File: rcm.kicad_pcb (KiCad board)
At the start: 2 copper layers, 140 x 70 mm, 158 parts, among them Y1 8MHz, Y2 32.768kHz

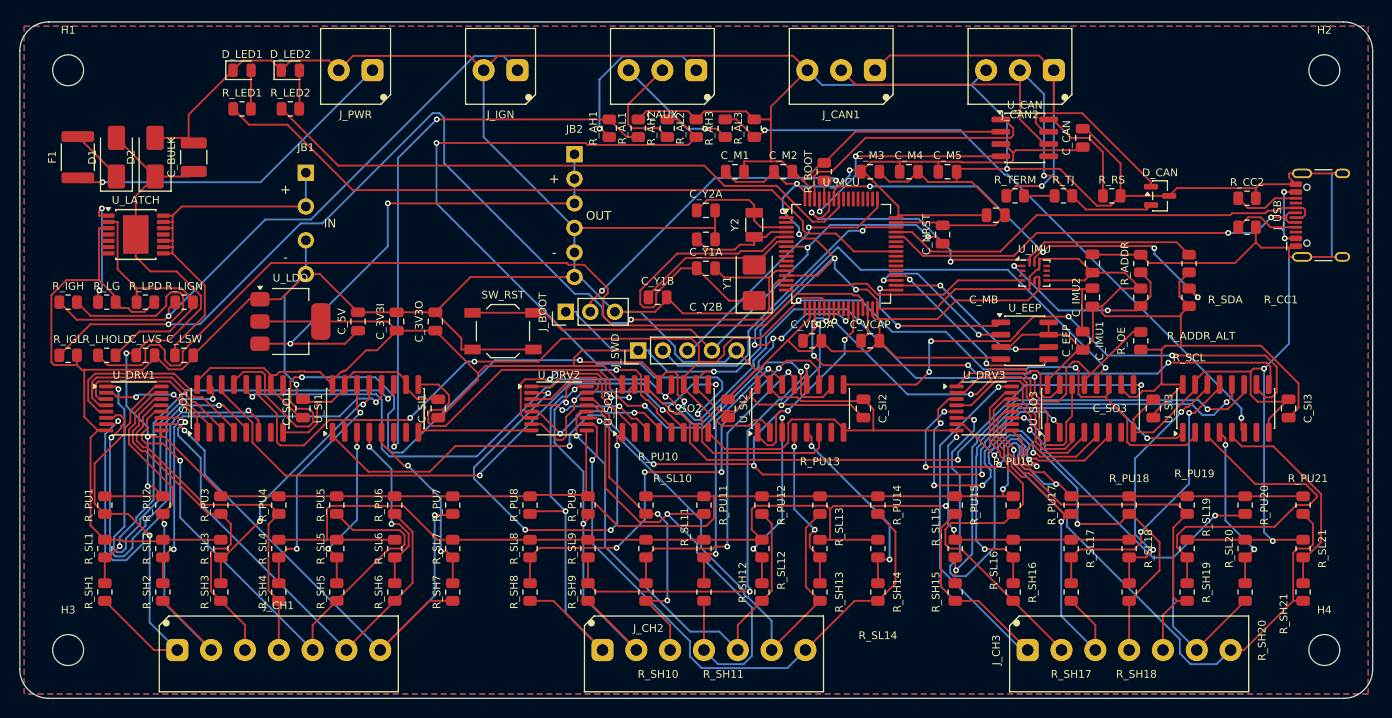
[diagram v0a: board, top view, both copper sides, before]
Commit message: rcm: resistor rows re-ordered, BOM sourced, manufacturing files out
Placement (user request): the three southern resistor rows keep their
6.0/10.5/15.0mm centre spacing, but R_PU moves to the southern row and
R_SH to the middle, both at rotation 0, with R_SL to the north row at
180. Laying them flat cleared nearly all the silkscreen crowding in the
south tiles.

BOM sourcing is complete - every line that gets assembled now has an
LCSC number. Four substitutions came out of it and are folded back into
gen_spec.py so the schematic agrees rather than the choice living only
in a side file:

  - AMS1117-3.3 for LD1117S33: JLC basic part, and pin-identical by
    construction (both symbols extend AP1117-15).
  - M95640 for 25LC640: $0.33 against $0.73-1.42 and better stocked,
    same 25-series SPI pinout the generic symbol already describes.
  - 60V PPTC over 30V: the SMAJ33A clamps near 53V.
  - 20pF for 12pF crystal load caps. This one was a genuine error, not
    a cost change: the 12.5pF crystal wants ~19pF, and 12pF ran the RTC
    about 22ppm fast - a minute a month. Also deletes a BOM line.

jlc_parts.json is rekeyed to 'value|footprint', which is what the BOM
script actually looks up; keyed by bare value it silently matched
nothing and would have produced an entirely unsourced BOM. The
footprint half earned its keep immediately by catching that the cheap
basic 8MHz crystal is HC-49S-SMD and would not fit the 5032 lands.
gen_spec.py now stamps an LCSC field onto every symbol from that same
file, and fails the build if a component has no line.

Two new shared tools: shrink_refs.py (0.8mm ref text on crowded parts,
which is what lets relocate_refs converge) and fix_marginal_clearance.py
(narrow rather than move segments that miss a rule by microns).

Board: 414/414 routed, 0 unconnected, 0 schematic parity. One clearance
violation survives at 1.3 microns short - deterministic, understood, and
documented in SPEC.md along with the three rejected fixes.

Gerbers export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
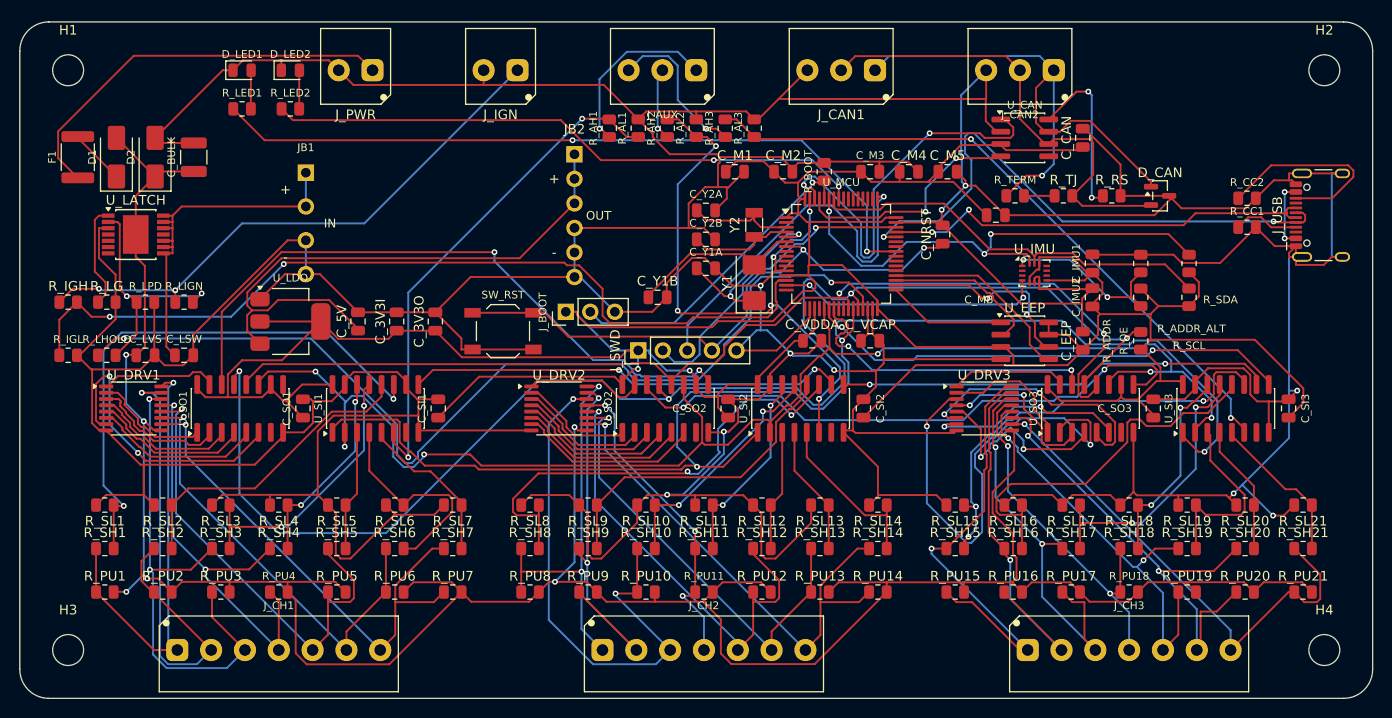
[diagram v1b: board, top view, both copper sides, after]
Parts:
- C_Y2A, C_Y2B: value 12pF -> 20pF
- U_EEP: value 25LC640 -> M95640
- U_LDO: value LD1117S33 -> AMS1117-3.3
- moved R_PU1 9.00 mm to (8.80, 59.0), turned to 0 degrees
- moved R_PU10 9.00 mm to (64.8, 59.0), turned to 0 degrees
- moved R_PU11 9.00 mm to (70.8, 59.0), turned to 0 degrees
- moved R_PU12 9.00 mm to (76.8, 59.0), turned to 0 degrees
- moved R_PU13 9.00 mm to (82.8, 59.0), turned to 0 degrees
- moved R_PU14 9.00 mm to (88.8, 59.0), turned to 0 degrees
- moved R_PU15 9.00 mm to (96.8, 59.0), turned to 0 degrees
- moved R_PU16 9.00 mm to (102.8, 59.0), turned to 0 degrees
- moved R_PU17 9.00 mm to (108.8, 59.0), turned to 0 degrees
- moved R_PU18 9.00 mm to (114.8, 59.0), turned to 0 degrees
- moved R_PU19 9.00 mm to (120.8, 59.0), turned to 0 degrees
- moved R_PU2 9.00 mm to (14.8, 59.0), turned to 0 degrees
- moved R_PU20 9.00 mm to (126.8, 59.0), turned to 0 degrees
- moved R_PU21 9.00 mm to (132.8, 59.0), turned to 0 degrees
- moved R_PU3 9.00 mm to (20.8, 59.0), turned to 0 degrees
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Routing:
- net +12V_P: track 220.1 -> 276.6 mm, vias 5 -> 6
- net ASNS2: track 96.4 -> 52.7 mm, vias 2 -> 4
- net DRV1: track 42.8 -> 12.0 mm, vias 2 -> 0
- net DRV9: track 40.8 -> 11.8 mm, vias 4 -> 0
- net IGN_SENSE: track 118.1 -> 90.4 mm
- net DRV6: track 44.2 -> 17.6 mm, vias 2 -> 0
- net GND: track 897.8 -> 873.1 mm, vias 7 -> 12
- net DRV20: track 50.9 -> 26.4 mm
- net SR_RCLK: track 133.6 -> 110.1 mm, vias 8 -> 2
- net CH10: track 33.7 -> 55.4 mm
- net +3V3: track 370.1 -> 391.5 mm, vias 9 -> 2
- net DRV17: track 30.7 -> 49.7 mm, vias 4 -> 2
- net CH11: track 51.1 -> 33.1 mm, vias 1 -> 3
- net CH3: track 35.8 -> 53.5 mm, vias 0 -> 2
- net SR_DI12: track 61.8 -> 45.5 mm
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- removed copper zone on B.Cu, net GND
- removed copper zone on F.Cu, net GND

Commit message: rcm: restore the GND pour - round 3 was routed without --zone
route_board.py's --zone defaults to empty, so omitting it produced a
fully routed, 0-unconnected, DRC-clean board with no copper pour on
either layer. Nothing in any report flagged it: an absent zone violates
no design rule, so DRC, the router summary and the netlist round-trip
were all clean and all silent. Caught by eye off the 3D view.

Re-routed with --zone GND:F.Cu --zone GND:B.Cu (2 zones, both filled,
33 polygons), then fix_starved_thermals.py set J_USB.A12, J_USB.B1 and
U_MCU.47 solid where thermal spokes came up short.

Board is otherwise where it was: 414/414 routed, 0 unconnected, 0
schematic parity, 26 silkscreen warnings and the same understood 1.3
micron clearance miss - which recurring across yet another independent
route further confirms it is deterministic geometry, not router noise.

Gerbers, BOM and CPL regenerated against the poured board; the previous
set had stale copper layers. Copper gerbers now carry the pour as G36
regions (F.Cu 27, B.Cu 6) and the zip goes 120kB -> 280kB.

Documented in CLAUDE.md and SPEC.md, including how to verify the pour
exists - counting top-level zone blocks, not the string '(zone', which
also matches the zone_connect inside every pad.

Co-Authored-By: Claude Opus 5 <noreply@anthropic.com>
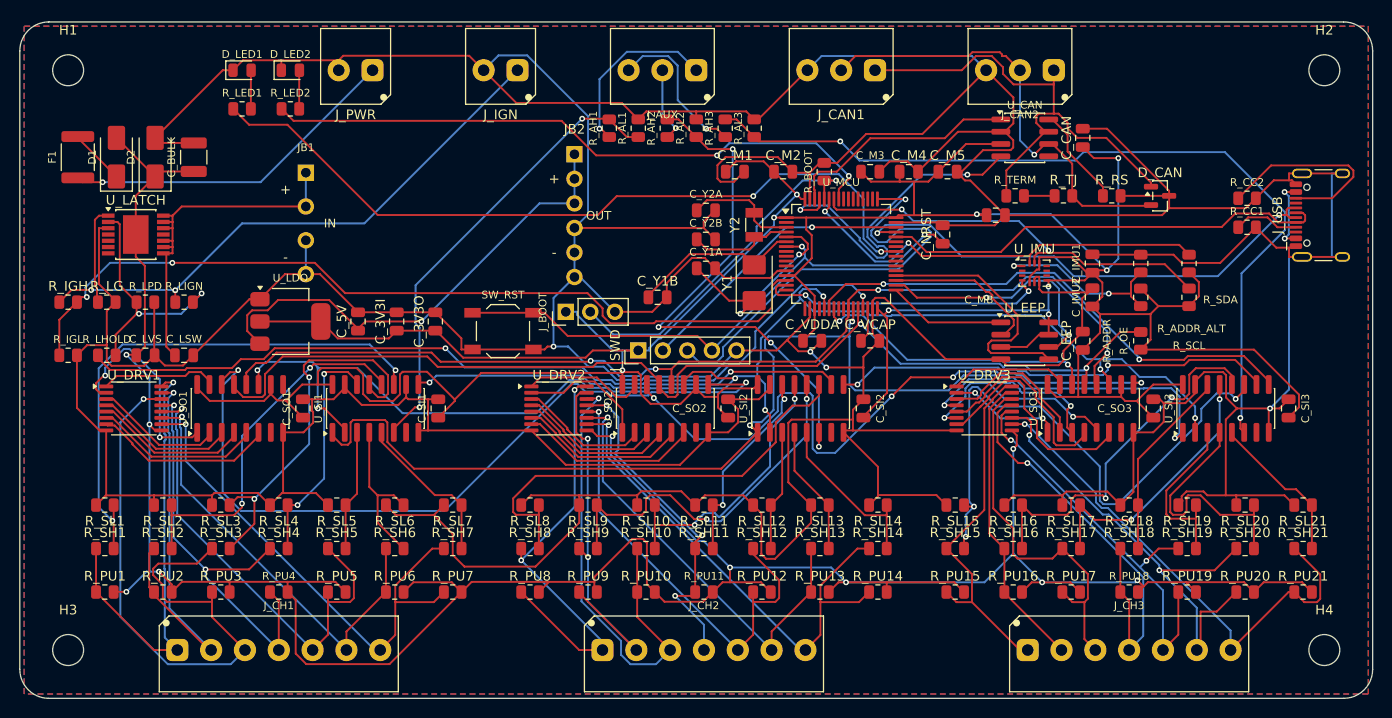
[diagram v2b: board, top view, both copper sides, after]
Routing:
- net SR_OE_N: track 149.5 -> 111.7 mm, vias 4 -> 2
- net DRV17: track 49.7 -> 15.8 mm, vias 2 -> 0
- net ASNS3: track 68.5 -> 87.5 mm
- net SR_PL: track 140.1 -> 122.3 mm
- net CAN_TX: track 41.7 -> 24.2 mm, vias 2 -> 0
- net SNS15: track 45.6 -> 60.5 mm
- net GND: track 873.1 -> 887.3 mm, vias 12 -> 4
- net SR_CH21: track 67.7 -> 81.3 mm
- net +12V_P: track 276.6 -> 289.9 mm, vias 6 -> 10
- net SNS20: track 13.5 -> 26.3 mm
- net USB_DM: track 58.9 -> 46.7 mm, vias 2 -> 0
- net LATCH_HOLD: track 101.5 -> 89.4 mm
- net +5V: track 61.9 -> 49.9 mm, vias 0 -> 1
- net DRV7: track 30.1 -> 18.8 mm, vias 2 -> 0
- net CAN_RX: track 24.3 -> 35.5 mm
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- added copper zone on B.Cu, net GND
- added copper zone on F.Cu, net GND

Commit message: rcm: latch part -> BTS7040-1EPZ, C534837 went to zero stock
JLC's quote priced 38 of 39 BOM lines; C534837 (BTS7040-1EPA) is
unbuyable. Swapped to C534838, BTS7040-1EPZ: same base part number, so
the Z is a temperature/variant grade rather than a different die and the
pinout is near-certain rather than resting on family convention. Same
PG-TSDSO-14-22 package, and better on both specs that matter - 19mOhm
against 36, and -40..+175C against +150.

The RCM:BTS70xx-1E symbol was built as a generic family part, which is
what made this a value-string change rather than a re-layout.

Stock is thin at ~10 pieces - enough for this run of 5 with spares. If it
goes, fall back to C534825 BTS7004-1EPP (~20k stock, overkill at
4.4mOhm/15A but harmless, same package and family pinout), which would
want a datasheet pinout check since it is not the same base part.

Rebuilt and re-routed WITH --zone GND:F.Cu --zone GND:B.Cu this time.
414/414 routed, 0 unconnected, 0 schematic parity, 2 filled GND pours,
and five pads set solid where thermal spokes came up short.

The 1.3 micron clearance miss is gone - this route avoids it - so the
board is now clean of every non-silkscreen violation, leaving 26 cosmetic
silkscreen warnings. That also corrects the earlier reading of it as
deterministic geometry: it was route-dependent, just not across the
routes tried at the time.

Gerbers, BOM and CPL regenerated.

Co-Authored-By: Claude Opus 5 <noreply@anthropic.com>
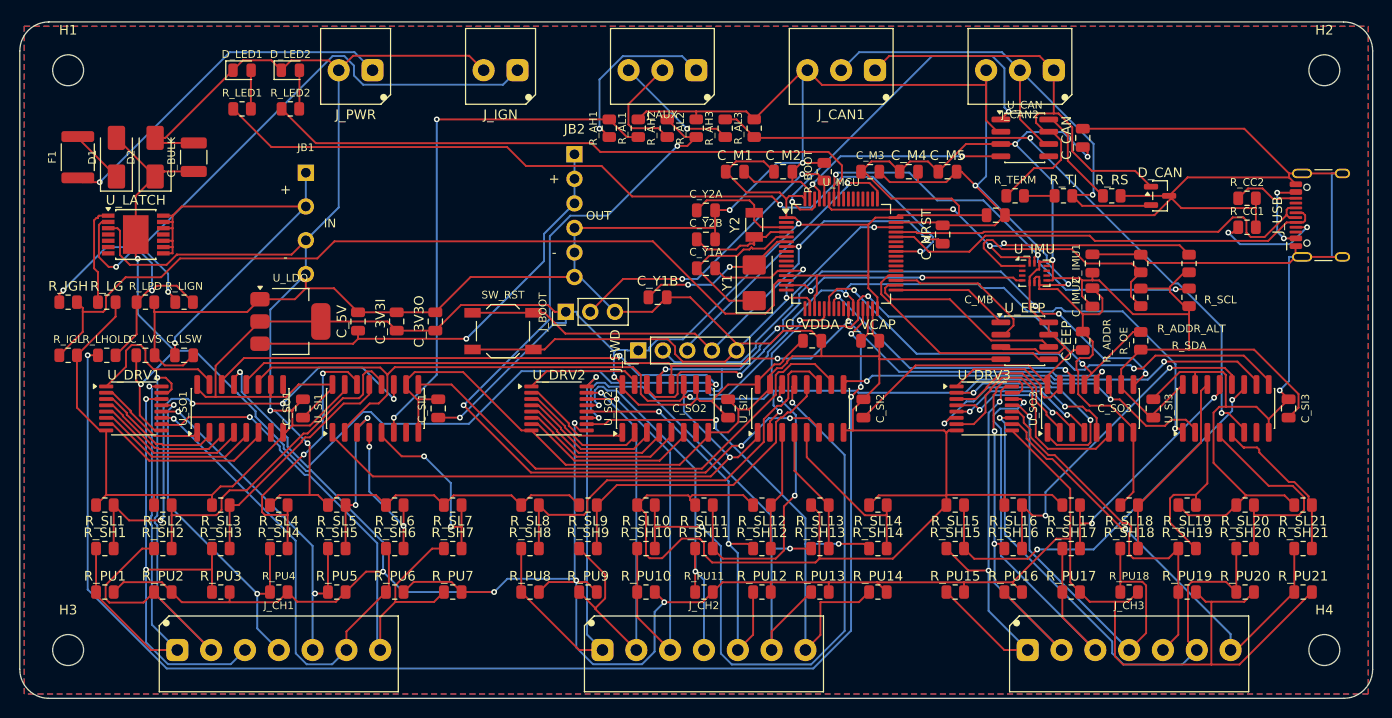
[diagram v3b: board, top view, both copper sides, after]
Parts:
- U_LATCH: value BTS7040-1EPA -> BTS7040-1EPZ
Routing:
- net GND: track 887.3 -> 944.1 mm, vias 4 -> 9
- net LATCH_HOLD: track 89.4 -> 144.0 mm, vias 2 -> 4
- net SNS10: track 28.9 -> 65.8 mm
- net ASNS2: track 56.2 -> 87.2 mm
- net SR_CH21: track 81.3 -> 54.7 mm
- net +12V_P: track 289.9 -> 311.0 mm, vias 10 -> 7
- net SWCLK: track 47.6 -> 28.5 mm
- net +3V3: track 397.7 -> 379.5 mm, vias 9 -> 6
- net SNS15: track 60.5 -> 42.3 mm, vias 3 -> 2
- net SR_OE_N: track 111.7 -> 127.3 mm, vias 2 -> 5
- net SNS3: track 39.9 -> 24.8 mm, vias 2 -> 0
- net ASNS3: track 87.5 -> 72.7 mm
- net CAN_TX: track 24.2 -> 38.5 mm, vias 0 -> 2
- net USB_CC2: track 21.1 -> 6.86 mm
- net CH3: track 64.0 -> 49.9 mm, vias 1 -> 2
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
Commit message: rcm: channel mode becomes a software table; add config DIP switch
Abandons the 21-DIP-switch plan and makes the board simpler instead.

The blocker was only ever the pull-UP: R_PU as 10k to +12V makes a blown
fuse read 2.531V and a good one 2.551V - both HIGH, 20mV apart, fuse
sensing dead. A 10k pull-DOWN does not, because the ~85 ohm relay coil
swamps it. All four states then read correctly with the SAME resistor
fitted on every channel:

  output, fuse good   2.530V HIGH      input, button open    0.000V LOW
  output, fuse blown  0.000V LOW       input, button closed  2.551V HIGH

So nothing is mode-dependent, there is nothing for hardware to select,
and in/out is purely a firmware table. R_PU is now fitted 10k to GND on
all 21 channels. That deleted the DIP array, the readback, the P-FET
rails and the south-half re-layout in one go.

Trade: buttons are positive-switched to +12V. Wetting current goes to
1.20mA (against 0.0094mA on the divider alone), and a chafed button wire
now reads 'not pressed' rather than phantom-activating.

Adds SW_CFG, one 8-way 1.27mm DIP in the top-right corner - the only free
10x10mm pocket, and next to J_CAN2 where the termination pole must reach.
Pos 1 CAN termination (passive, parallels R_TJ); pos 2-6 role, address
x2, bitrate, IMU publish enable, on PC0-PC4 using the STM32's internal
pull-ups so no external resistors are needed. These are the settings that
cannot be fixed over the bus once wrong.

Positions 7-8 are left unconnected deliberately: routing two more nets
from that corner across the CAN/IMU corridor is what tipped the board
from routable to not (3 nets failed, then 1). Dropping them fixed it.

426/426 routed, 0 unconnected, 0 schematic parity, 2 filled GND pours,
25 cosmetic silkscreen warnings and no electrical violations at all.
BOM 40 lines all sourced, CPL 149 placements.

VERIFY the DIP land before ordering - standard 1.27mm 8-position
gull-wing footprint, part not checked against a drawing.

Co-Authored-By: Claude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
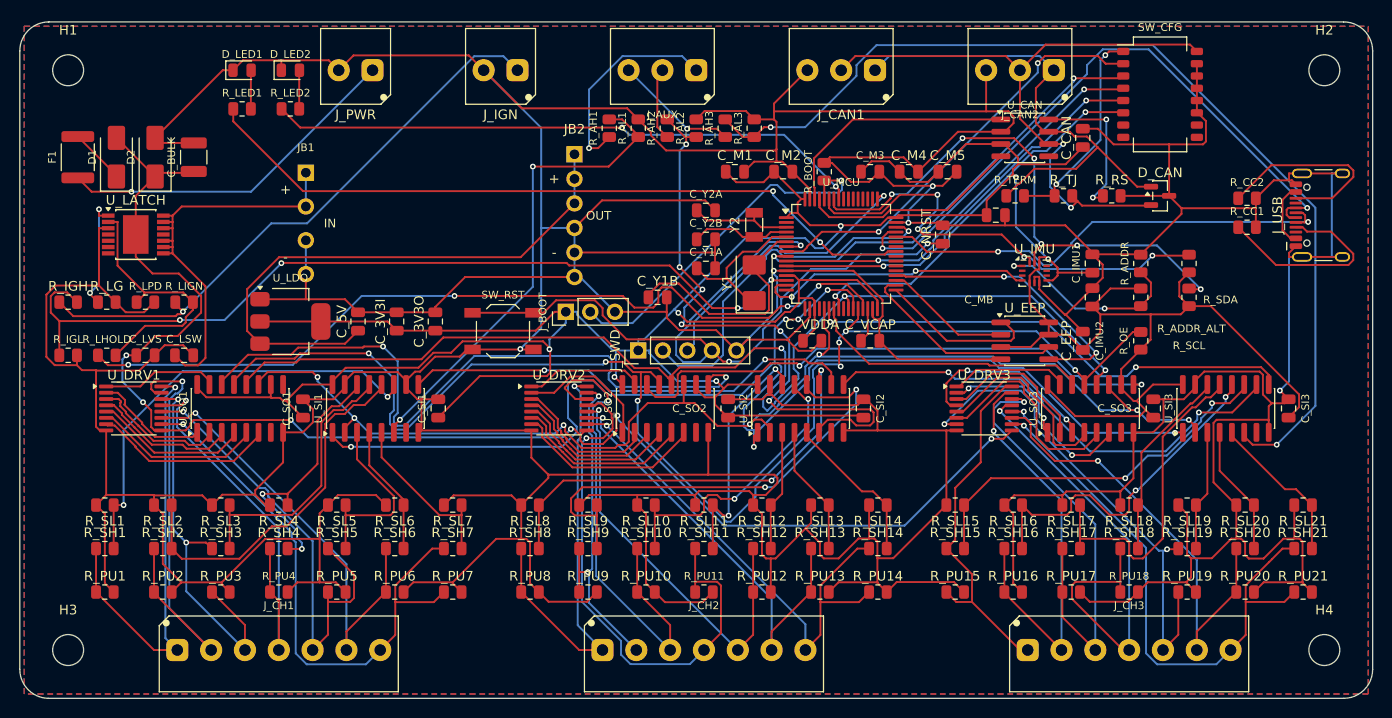
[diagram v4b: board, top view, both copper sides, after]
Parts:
- added SW_CFG: CFG_DIP, Button_Switch_SMD:SW_DIP_SPSTx08_Slide_KingTek_DSHP08TS_W7.62mm_P1.27mm, F.Cu at (118.0, 7.50)
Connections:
- R_PU1 pad 2: +12V_P -> GND
- R_PU10 pad 2: +12V_P -> GND
- R_PU11 pad 2: +12V_P -> GND
- R_PU12 pad 2: +12V_P -> GND
- R_PU13 pad 2: +12V_P -> GND
- R_PU14 pad 2: +12V_P -> GND
- R_PU15 pad 2: +12V_P -> GND
- R_PU16 pad 2: +12V_P -> GND
- R_PU17 pad 2: +12V_P -> GND
- R_PU18 pad 2: +12V_P -> GND
- R_PU19 pad 2: +12V_P -> GND
- R_PU2 pad 2: +12V_P -> GND
- R_PU20 pad 2: +12V_P -> GND
- R_PU21 pad 2: +12V_P -> GND
- R_PU3 pad 2: +12V_P -> GND
- R_PU4 pad 2: +12V_P -> GND
- R_PU5 pad 2: +12V_P -> GND
- R_PU6 pad 2: +12V_P -> GND
- R_PU7 pad 2: +12V_P -> GND
- R_PU8 pad 2: +12V_P -> GND
- R_PU9 pad 2: +12V_P -> GND
- U_MCU pad 10: unconnected-(U_MCU-PC2-Pad10) -> CFG_ADDR1
- U_MCU pad 11: unconnected-(U_MCU-PC3-Pad11) -> CFG_BAUD
- U_MCU pad 24: unconnected-(U_MCU-PC4-Pad24) -> CFG_IMU_EN
- U_MCU pad 8: unconnected-(U_MCU-PC0-Pad8) -> CFG_ROLE
- U_MCU pad 9: unconnected-(U_MCU-PC1-Pad9) -> CFG_ADDR0
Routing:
- net +12V_P: track 311.0 -> 151.4 mm, vias 7 -> 6
- net GND: track 944.1 -> 1068.3 mm, vias 9 -> 5
- net LATCH_HOLD: track 144.0 -> 89.0 mm
- net CFG_ADDR0: track 0.00 -> 45.8 mm, vias 0 -> 2
- net CFG_ROLE: track 0.00 -> 44.2 mm, vias 0 -> 2
- net CFG_ADDR1: track 0.00 -> 42.6 mm, vias 0 -> 2
- net CFG_BAUD: track 0.00 -> 42.3 mm, vias 0 -> 2
- net CFG_IMU_EN: track 0.00 -> 39.8 mm, vias 0 -> 2
- net SNS10: track 65.8 -> 30.3 mm
- net ASNS3: track 72.7 -> 103.7 mm
- net NRST: track 59.1 -> 83.9 mm, vias 2 -> 3
- net ASNS2: track 87.2 -> 63.4 mm, vias 4 -> 6
- net USB_DP: track 46.3 -> 66.4 mm, vias 0 -> 2
- net SR_RCLK: track 99.1 -> 118.2 mm
- net CAN_TERM: track 3.18 -> 21.9 mm, vias 0 -> 2
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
